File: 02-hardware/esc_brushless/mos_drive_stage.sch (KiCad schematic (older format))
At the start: 31 parts

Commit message: Schematics v1.0 - Architecture, microcontroler, global interconnections and IO
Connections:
- net 3.3V_MCU: no longer C?.1, L?.2, R?.1
- new net 5_VCC: C?.1, L?.2, R?.1
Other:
- moved on the sheet: C?, D?, L?, R?, U?

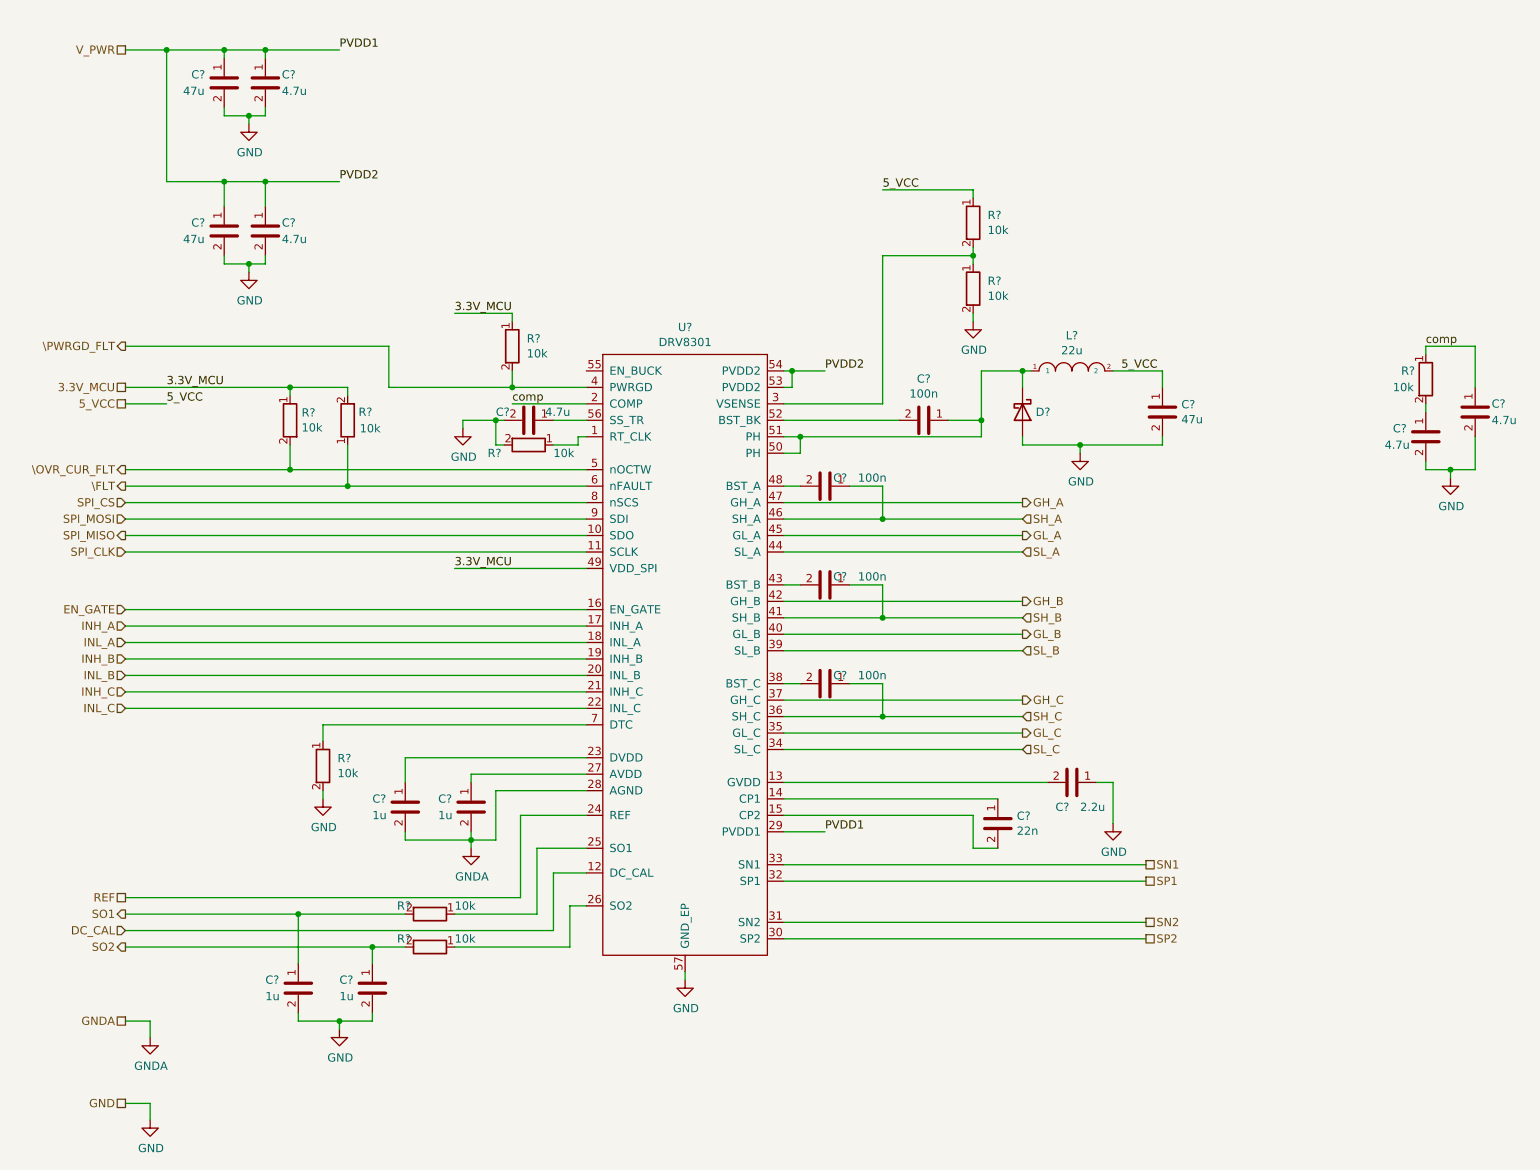
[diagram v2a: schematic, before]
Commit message: Schematics v1.0 - Fix DRC issues
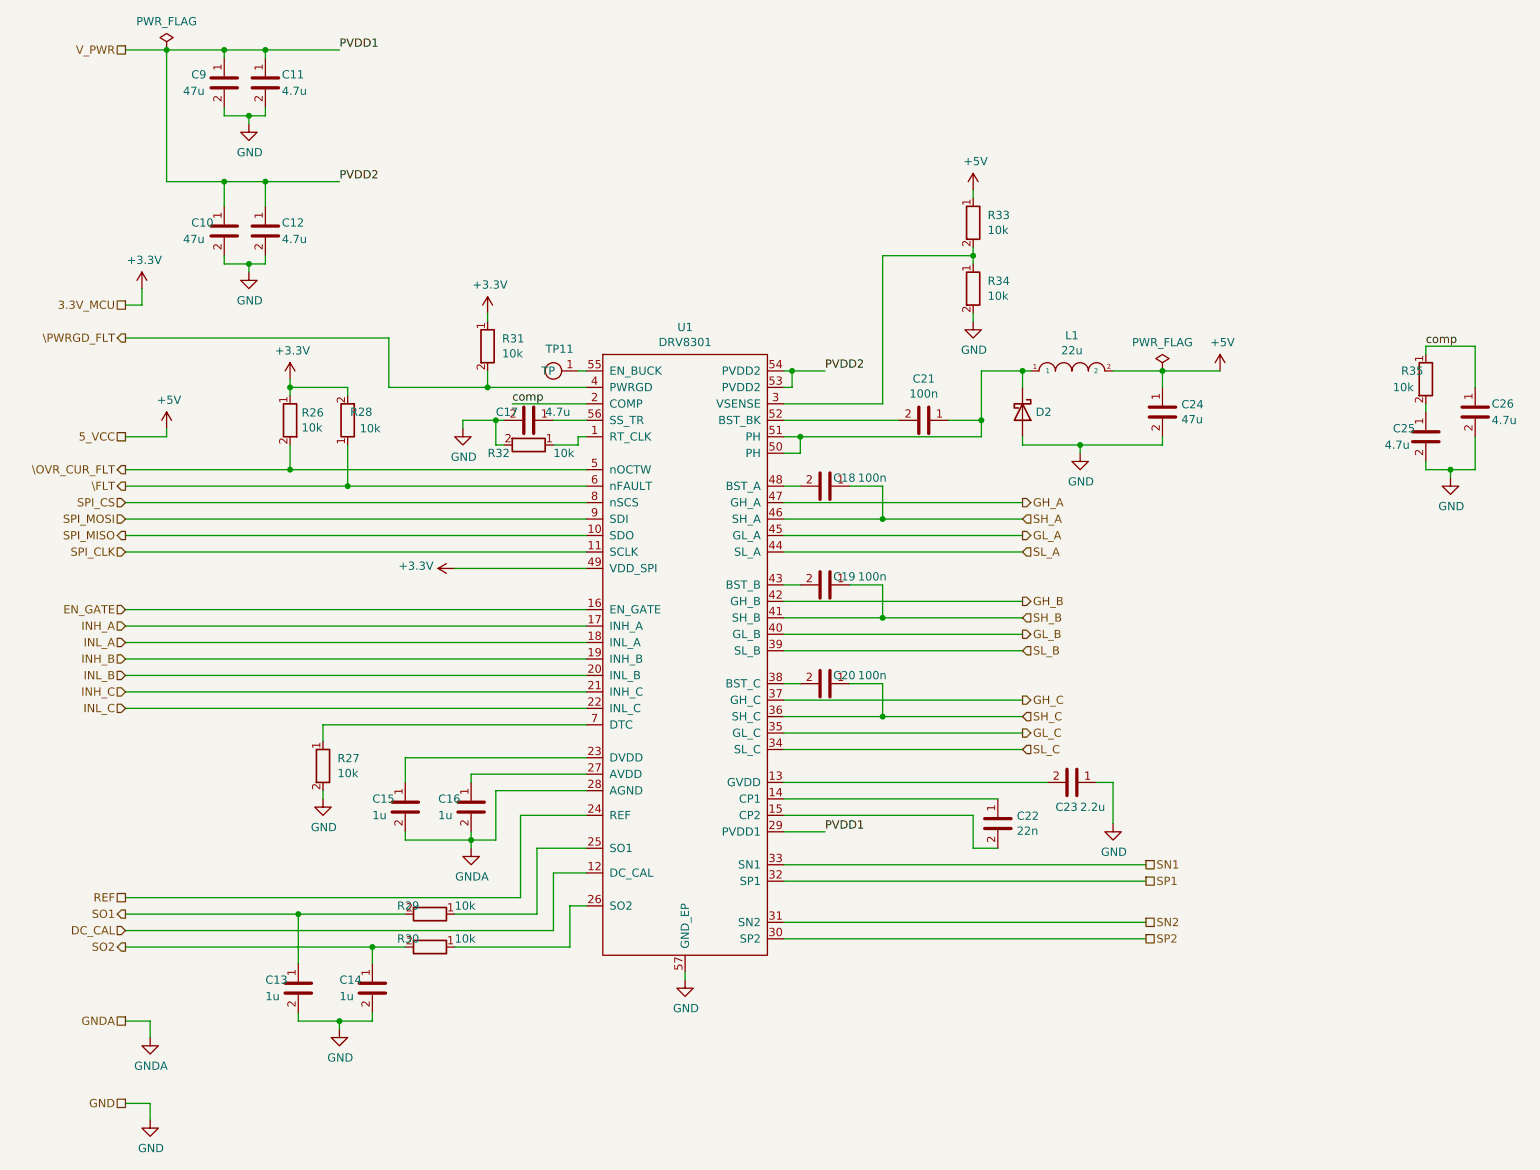
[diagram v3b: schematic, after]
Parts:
- removed U?: DRV8301, p_Package_SO:HTSSOP-56-1EP_6.1x14mm_P0.5mm_EP3.61x6.35mm.kicad_mod, symbol p_Driver_IC:DRV8301
- added TP11: test_point, p_Package_Misc:TP_SMD_1.25mm, symbol p_Misc:test_point
- added U1: DRV8301, p_Package_SO:HTSSOP-56-1EP_6.1x14mm_P0.5mm_EP3.61x6.35mm.kicad_mod, symbol p_Driver_IC:DRV8301
- gave numbers to parts that had none: 30
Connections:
- net DC_CAL: now also U1.12 (DC_CAL)
- net EN_GATE: now also U1.16 (EN_GATE)
- net GH_A: now also U1.47 (GH_A)
- net GH_B: now also U1.42 (GH_B)
- net GH_C: now also U1.37 (GH_C)
- net GL_A: now also U1.45 (GL_A)
- net GL_B: now also U1.40 (GL_B)
- net GL_C: now also U1.35 (GL_C)
- net GND: now also U1.57 (GND_EP)
- net GNDA: now also U1.28 (AGND)
- net INH_A: now also U1.17 (INH_A)
- net INH_B: now also U1.19 (INH_B)
- net INH_C: now also U1.21 (INH_C)
- net INL_A: now also U1.18 (INL_A)
- net INL_B: now also U1.20 (INL_B)
- net INL_C: now also U1.22 (INL_C)
- net REF: now also U1.24 (REF)
- net SH_A: now also U1.46 (SH_A)
- net SH_B: now also U1.41 (SH_B)
- net SH_C: now also U1.36 (SH_C)
- net SL_A: now also U1.44 (SL_A)
- net SL_B: now also U1.39 (SL_B)
- net SL_C: now also U1.34 (SL_C)
- net SN1: now also U1.33 (SN1)
- net SN2: now also U1.31 (SN2)
- net SP1: now also U1.32 (SP1)
- net SP2: now also U1.30 (SP2)
- net SPI_CLK: now also U1.11 (SCLK)
- net SPI_CS: now also U1.8 (nSCS)
- net SPI_MISO: now also U1.10 (SDO)
- net SPI_MOSI: now also U1.9 (SDI)
- net V_PWR: now also U1.29 (PVDD1), U1.53 (PVDD2), U1.54 (PVDD2)
- net \FLT: now also U1.6 (nFAULT)
- net \OVR_CUR_FLT: now also U1.5 (nOCTW)
- net \PWRGD_FLT: now also U1.4 (PWRGD)
- net comp: now also U1.2 (COMP)
- net at R32.1: now also U1.1 (RT_CLK)
- net at R27.1: now also U1.7 (DTC)
- net at C15.1: now also U1.23 (DVDD)
- net at C22.1: now also U1.14 (CP1)
- net at C22.2: now also U1.15 (CP2)
- net at C23.2: now also U1.13 (GVDD)
- net at R29.1: now also U1.25 (SO1)
- net at R30.1: now also U1.26 (SO2)
- net at C16.1: now also U1.27 (AVDD)
- net at R33.2, R34.1: now also U1.3 (VSENSE)
- net at C20.2: now also U1.38 (BST_C)
- net at C19.2: now also U1.43 (BST_B)
- net at C18.2: now also U1.48 (BST_A)
- net at C21.1, D2.1 (K), L1.1: now also U1.50 (PH), U1.51 (PH)
- net at C21.2: now also U1.52 (BST_BK)
- net at C17.1: now also U1.56 (SS_TR)
- net 3.3V_MCU renamed +3V3
- net +3V3: now also U1.49 (VDD_SPI)
- net 5_VCC renamed +5V
- new net: TP11.1 (TP), U1.55 (EN_BUCK)
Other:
- moved on the sheet: R31

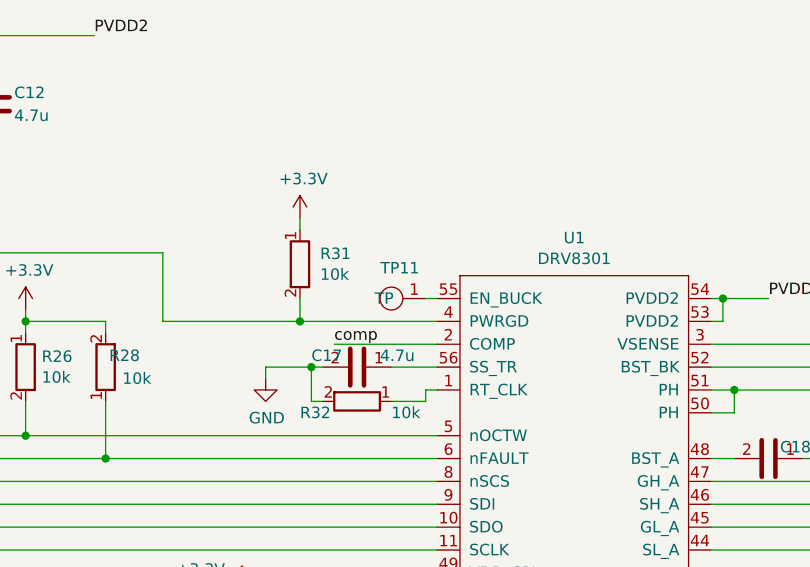
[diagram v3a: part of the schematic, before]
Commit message: Schematics v1.0 - Remove some options and test points
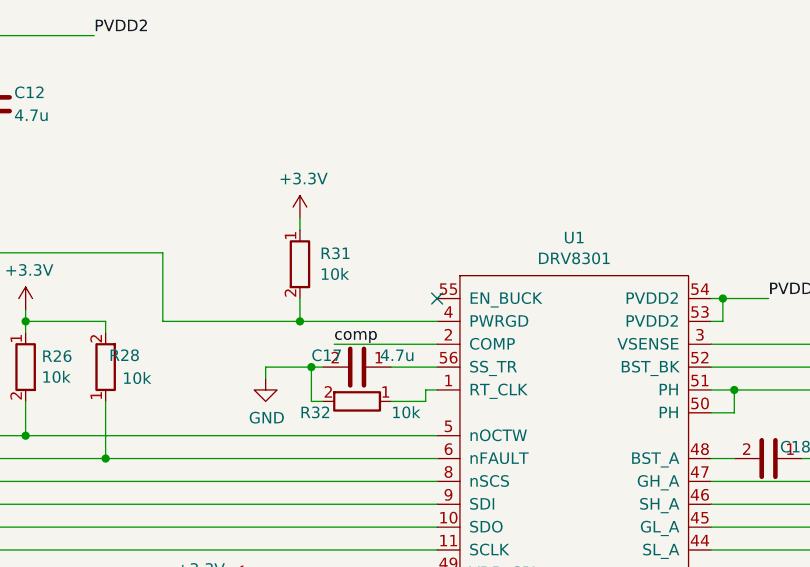
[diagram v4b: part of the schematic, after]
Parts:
- removed TP11: test_point, p_Package_Misc:TP_SMD_1.25mm, symbol p_Misc:test_point
- U1: footprint p_Package_SO:HTSSOP-56-1EP_6.1x14mm_P0.5mm_EP3.61x6.35mm.kicad_mod -> p_Package_SO:HTSSOP-56-1EP_6.1x14mm_P0.5mm_EP3.61x6.35mm
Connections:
- no-connect marks 0 -> 1
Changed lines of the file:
@@
 Wire Wire Line
 	2750 7150 2750 7250
-$Comp
-L p_Misc:test_point TP11
-U 1 1 60D230AE
-P 5250 2700
-F 0 "TP11" H 5237 2833 50  0000 C CNN
-F 1 "test_point" H 5237 2834 50  0001 C CNN
-F 2 "p_Package_Misc:TP_SMD_1.25mm" H 5250 2500 50  0001 C CNN
-F 3 "" H 5250 2700 50  0001 C CNN
-	1    5250 2700
-	1    0    0    -1
-$EndComp
-Wire Wire Line
-	5350 2700 5400 2700
-Connection ~ 4800 2800
-Wire Wire Line
-	4800 2800 5400 2800
 Wire Wire Line
 	4200 2800 4800 2800
@@
 F 0 "U1" H 6000 5565 50  0000 C CNN
 F 1 "DRV8301" H 6000 5474 50  0000 C CNN
-F 2 "p_Package_SO:HTSSOP-56-1EP_6.1x14mm_P0.5mm_EP3.61x6.35mm.kicad_mod" H 5950 2800 50  0001 C CNN
+F 2 "p_Package_SO:HTSSOP-56-1EP_6.1x14mm_P0.5mm_EP3.61x6.35mm" H 5950 2800 50  0001 C CNN
 F 3 "" H 5950 4450 50  0001 C CNN
 	1    6000 4000
@@
 $EndComp
 $Comp
-L power:+3.3V #PWR?
+L power:+3.3V #PWR0114
 U 1 1 60E7494C
 P 2700 2200
-F 0 "#PWR?" H 2700 2050 50  0001 C CNN
+F 0 "#PWR0114" H 2700 2050 50  0001 C CNN
 F 1 "+3.3V" H 2715 2373 50  0000 C CNN
 F 2 "" H 2700 2200 50  0001 C CNN
@@
 	2700 2300 2600 2300
 $Comp
-L power:+3.3V #PWR?
+L power:+3.3V #PWR0115
 U 1 1 60E8507B
 P 4800 2350
-F 0 "#PWR?" H 4800 2200 50  0001 C CNN
+F 0 "#PWR0115" H 4800 2200 50  0001 C CNN
 F 1 "+3.3V" H 4815 2523 50  0000 C CNN
 F 2 "" H 4800 2350 50  0001 C CNN
@@
 $EndComp
 $Comp
-L power:+3.3V #PWR?
+L power:+3.3V #PWR0116
 U 1 1 60E89F1B
 P 3600 2750
-F 0 "#PWR?" H 3600 2600 50  0001 C CNN
+F 0 "#PWR0116" H 3600 2600 50  0001 C CNN
 F 1 "+3.3V" H 3615 2923 50  0000 C CNN
 F 2 "" H 3600 2750 50  0001 C CNN
@@
 Connection ~ 3600 2800
 $Comp
-L power:+3.3V #PWR?
+L power:+3.3V #PWR0117
 U 1 1 60EA0111
 P 4600 3900
-F 0 "#PWR?" H 4600 3750 50  0001 C CNN
+F 0 "#PWR0117" H 4600 3750 50  0001 C CNN
 F 1 "+3.3V" V 4615 4028 50  0000 L CNN
 F 2 "" H 4600 3900 50  0001 C CNN
@@
 	0    -1   -1   0
 $EndComp
+Connection ~ 4800 2800
+Wire Wire Line
+	4800 2800 5400 2800
+NoConn ~ 5400 2700
 $EndSCHEMATC
